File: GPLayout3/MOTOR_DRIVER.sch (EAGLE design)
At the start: 94 parts, among them T1 2N2222, T2 2N2222, U7 ATMEGA328P_TQFP, Y1 16MHz

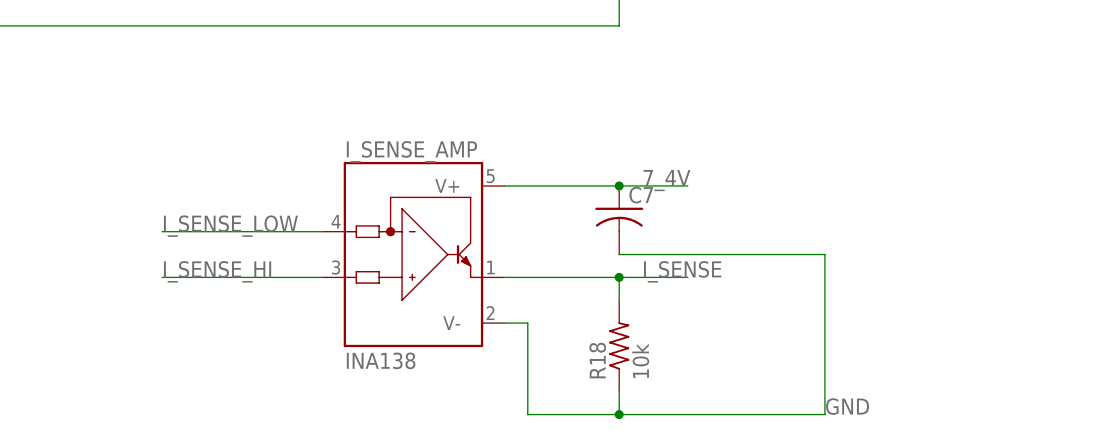
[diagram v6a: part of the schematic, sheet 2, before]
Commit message: Fixed errors on top board and moved current sense amp to top
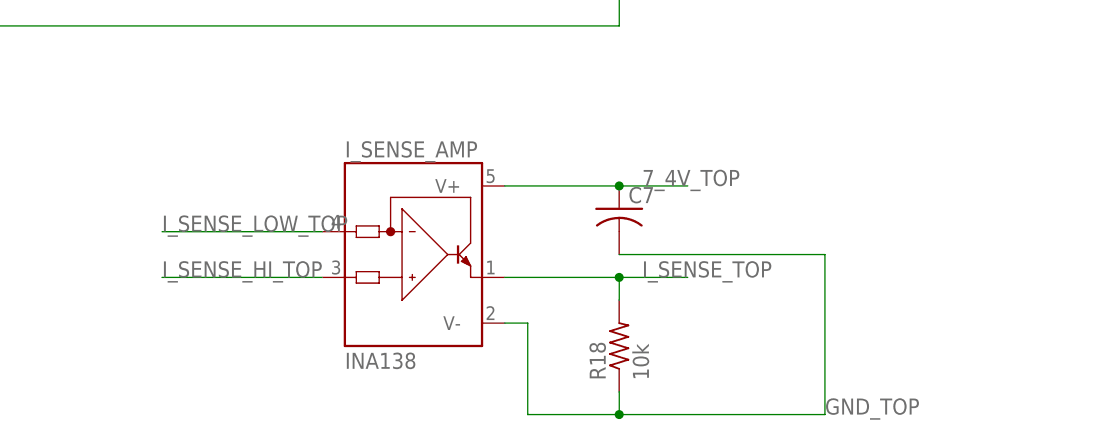
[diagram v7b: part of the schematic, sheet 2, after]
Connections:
- new net I_SENSE_TOP: I_SENSE_AMP.OUT, R18.2, SV6.3
- net 7_4V: no longer C7.1, I_SENSE_AMP.V+
- net 7_4V_TOP: now also C7.1, I_SENSE_AMP.V+
- net GND: no longer C7.2, I_SENSE_AMP.V-, R18.1
- net GND_TOP: now also C7.2, I_SENSE_AMP.V-, R18.1
- net I_SENSE: no longer I_SENSE_AMP.OUT, R18.2
- net I_SENSE_HI: no longer I_SENSE_AMP.IN+
- net I_SENSE_HI_TOP: now also I_SENSE_AMP.IN+; no longer SV5.2
- net I_SENSE_LOW: no longer I_SENSE_AMP.IN-
- net I_SENSE_LOW_TOP: now also I_SENSE_AMP.IN-; no longer SV5.1

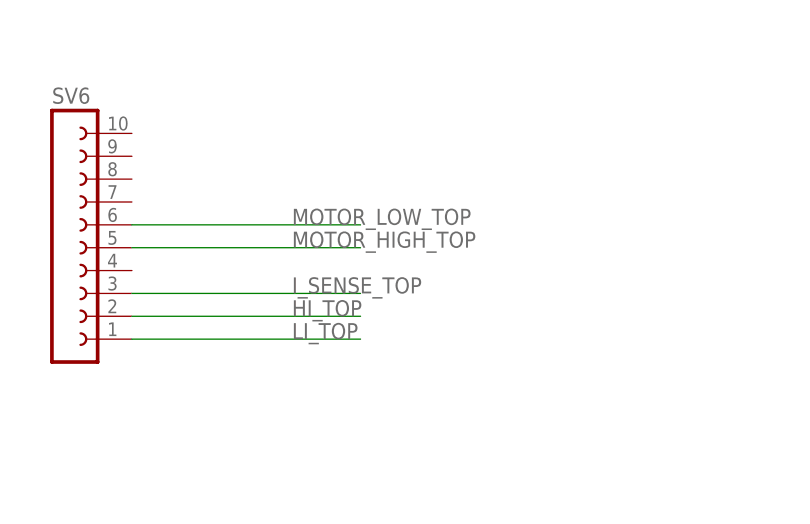
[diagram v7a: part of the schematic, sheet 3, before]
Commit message: Fixed missing motor_high_top pin, now I_SENSE_LOW_TOP
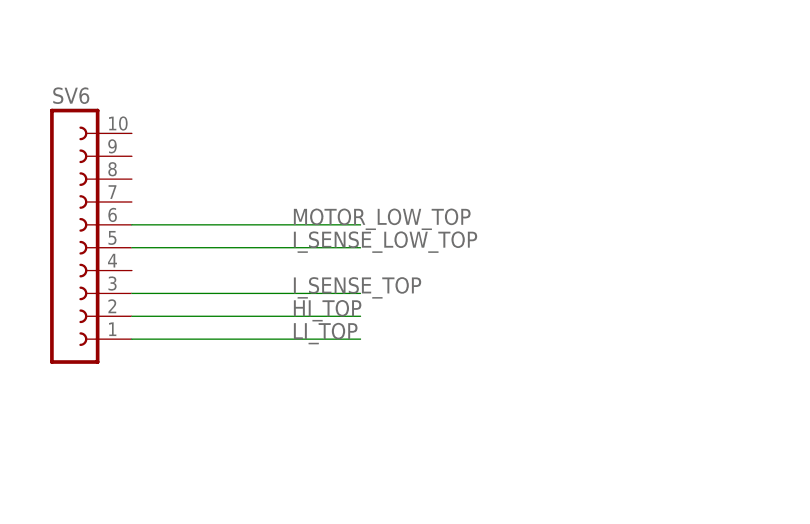
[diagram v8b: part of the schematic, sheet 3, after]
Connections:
- removed net MOTOR_HIGH_TOP: SV6.5
- net I_SENSE_LOW_TOP: now also SV6.5
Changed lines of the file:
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@@
 </segment>
 </net>
-<net name="MOTOR_HIGH_TOP" class="0">
+<net name="I_SENSE_LOW_TOP" class="0">
 <segment>
 <pinref part="SV6" gate="G$1" pin="5"/>
